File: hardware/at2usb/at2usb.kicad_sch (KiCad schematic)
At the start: 8 parts, among them J1 AT (PS/2) keyboard, J2 UART, J3 USB connector breakout board, J4 Programmer, U1 PIC16F1459-IP

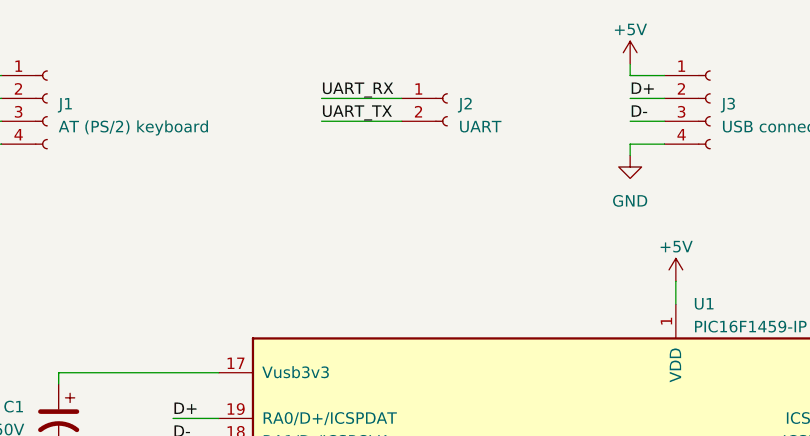
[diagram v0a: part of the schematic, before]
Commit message: Add gnd pin next to uart pins
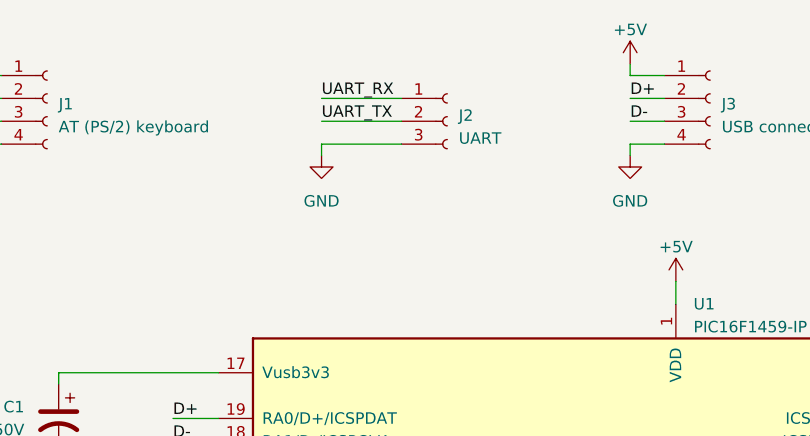
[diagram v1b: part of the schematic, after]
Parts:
- removed J2: UART, Connector_PinHeader_2.54mm:PinHeader_1x02_P2.54mm_Vertical, symbol Connector:Conn_01x02_Socket
- added J2: UART, Connector_PinHeader_2.54mm:PinHeader_1x03_P2.54mm_Vertical, symbol Connector:Conn_01x03_Socket
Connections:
- net GND: now also J2.3 (Pin_3)
- net UART_RX: now also J2.1 (Pin_1)
- net UART_TX: now also J2.2 (Pin_2)
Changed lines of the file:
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@@
+    (stroke (width 0) (type default))
+  )
+  (wire (pts (xy 69.85 27.94) (xy 69.85 29.21))
     (stroke (width 0) (type default))
   )
@@
   )
   (wire (pts (xy 109.22 88.9) (xy 109.22 93.98))
+    (stroke (width 0) (type default))
+  )
+  (wire (pts (xy 78.74 27.94) (xy 69.85 27.94))
     (stroke (width 0) (type default))
   )
@@
     )
   )
-  (symbol (lib_id "Connector:Conn_01x02_Socket") (at 83.82 22.86 0) (unit 1)
-    (in_bom yes) (on_board yes) (dnp no)
-    (property "Reference" "J2" (at 85.09 23.495 0)
-      (effects (font (size 1.27 1.27)) (justify left))
-    )
-    (property "Value" "UART" (at 85.09 26.035 0)
-      (effects (font (size 1.27 1.27)) (justify left))
-    )
-    (property "Footprint" "Connector_PinHeader_2.54mm:PinHeader_1x02_P2.54mm_Vertical" (at 83.82 22.86 0)
-      (effects (font (size 1.27 1.27)) hide)
-    )
-    (property "Datasheet" "~" (at 83.82 22.86 0)
-      (effects (font (size 1.27 1.27)) hide)
-    )
-    (pin "1")
-    (pin "2")
-    (instances
-      (project "at2usb"
-        (path "/c9401900-ddb3-4546-8434-70a09aaeb18a"
-          (reference "J2") (unit 1)
-        )
-      )
-    )
-  )
   (symbol (lib_id "power:+5V") (at 104.14 19.05 0) (unit 1)
     (in_bom yes) (on_board yes) (dnp no) (fields_autoplaced)
@@
     )
   )
+  (symbol (lib_id "power:GND") (at 69.85 29.21 0) (unit 1)
+    (in_bom yes) (on_board yes) (dnp no) (fields_autoplaced)
+    (property "Reference" "#PWR014" (at 69.85 35.56 0)
+      (effects (font (size 1.27 1.27)) hide)
+    )
+    (property "Value" "GND" (at 69.85 34.29 0)
+      (effects (font (size 1.27 1.27)))
+    )
+    (property "Footprint" "" (at 69.85 29.21 0)
+      (effects (font (size 1.27 1.27)) hide)
+    )
+    (property "Datasheet" "" (at 69.85 29.21 0)
+      (effects (font (size 1.27 1.27)) hide)
+    )
+    (pin "1")
+    (instances
+      (project "at2usb"
+        (path "/c9401900-ddb3-4546-8434-70a09aaeb18a"
+          (reference "#PWR014") (unit 1)
+        )
+      )
+    )
+  )
   (symbol (lib_id "power:GND") (at 40.64 66.04 0) (unit 1)
     (in_bom yes) (on_board yes) (dnp no) (fields_autoplaced)
@@
         )
       )
+    )
+  )
+  (symbol (lib_id "Connector:Conn_01x03_Socket") (at 83.82 25.4 0) (unit 1)
+    (in_bom yes) (on_board yes) (dnp no) (fields_autoplaced)
+    (property "Reference" "J2" (at 85.09 24.765 0)
+      (effects (font (size 1.27 1.27)) (justify left))
+    )
+    (property "Value" "UART" (at 85.09 27.305 0)
+      (effects (font (size 1.27 1.27)) (justify left))
+    )
+    (property "Footprint" "Connector_PinHeader_2.54mm:PinHeader_1x03_P2.54mm_Vertical" (at 83.82 25.4 0)
+      (effects (font (size 1.27 1.27)) hide)
+    )
+    (property "Datasheet" "~" (at 83.82 25.4 0)
+      (effects (font (size 1.27 1.27)) hide)
+    )
+    (pin "1")
+    (pin "2")
+    (pin "3")
+    (instances
+      (project "at2usb"
+        (path "/c9401900-ddb3-4546-8434-70a09aaeb18a"
+          (reference "J2") (unit 1)
+        )
+      )

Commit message: Add MCLR pull-up resistor in schematic, remove UART RX
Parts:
- added R1: 10k, Resistor_THT:R_Axial_DIN0207_L6.3mm_D2.5mm_P2.54mm_Vertical, symbol Device:R_US
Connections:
- net +5V: now also R1.1
- net /MCLR: now also R1.2
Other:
- moved on the sheet: C2, C3
